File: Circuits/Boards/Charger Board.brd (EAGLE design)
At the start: 63.5 x 50.8 mm, 67 parts, among them CON1 ISP(2X3), CON10 HEADER_3X1, CON11 HEADER_3X1, CON12 HEADER_3X1, CON3 HEADER_3X1, CON4 HEADER_3X1, CON5 HEADER_3X1, CON6 HEADER_3X1, CON7 HEADER_3X1, CON8 HEADER_3X1, CON9 HEADER_3X1, IC1 NCP1117DT33G, T1 NPN2N2222, T2 NPN2N2222, T3 SI4421DY, U1 ATMEGA324P, U2 ACS711

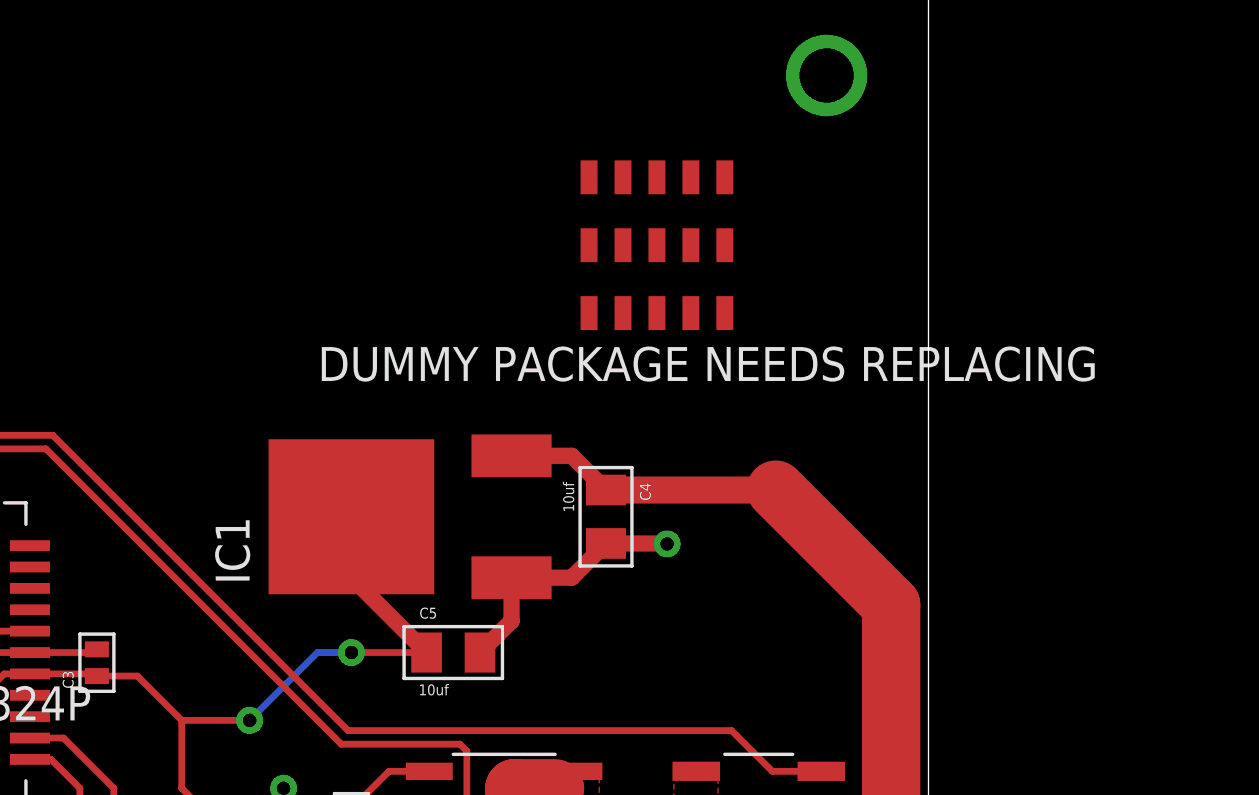
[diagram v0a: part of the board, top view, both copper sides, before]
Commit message: 
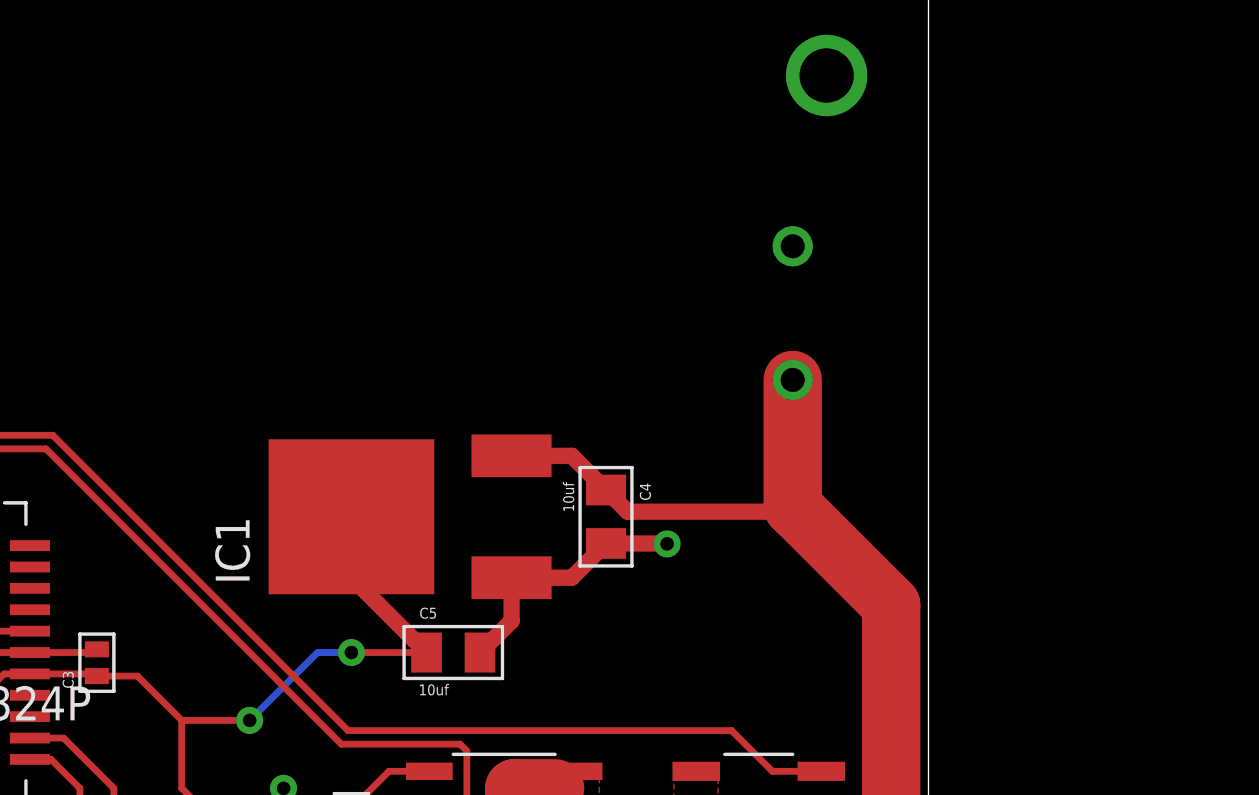
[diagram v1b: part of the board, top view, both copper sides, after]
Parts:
- removed S1: ROCKER_SWITCH, Mechanical:DUMMY
- added CON2: SCREWTERMINAL_1X2, Mechanical:SCREWTERMINAL_1X2
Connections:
- removed net VIN: S1.P$2
- net +5V: now also CON2.1; no longer S1.P$3
- net GND: now also CON2.2
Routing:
- net +5V: track 28.8 -> 33.8 mm
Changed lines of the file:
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@@
 <element name="R27" library="Passive" package="0603" value="470" x="52.705" y="12.7" rot="R90"/>
 <element name="R28" library="Passive" package="0603" value="" x="8.89" y="35.56" rot="R180"/>
-<element name="S1" library="Mechanical" package="DUMMY" value="ROCKER_SWITCH" x="53.34" y="40.64" rot="R180"/>
 <element name="U2" library="PowerIC" package="8SOIC" value="ACS711" x="47.625" y="19.05" rot="R90"/>
 <element name="C1" library="Passive" package="0603" value=".1uf" x="41.91" y="19.05" rot="R90"/>
@@
 <element name="H3" library="Mechanical" package="MOUNTINGHOLE" value="MOUNTINGHOLE" x="59.69" y="46.99"/>
 <element name="H4" library="Mechanical" package="MOUNTINGHOLE" value="MOUNTINGHOLE" x="59.69" y="3.81"/>
+<element name="CON2" library="Mechanical" package="SCREWTERMINAL_1X2" value="SCREWTERMINAL_1X2" x="58.42" y="38.1" rot="R90"/>
 </elements>
 <signals>
@@
 <wire x1="11.16" y1="37.1" x2="11.43" y2="36.83" width="0.254" layer="1"/>
 <via x="11.43" y="36.83" extent="1-16" drill="0.508"/>
+<contactref element="CON2" pad="2"/>
 <wire x1="9.84" y1="37.1" x2="-18.05" y2="68.58" width="0" layer="19" extent="1-1"/>
 <wire x1="-70.8" y1="61.96" x2="-18.05" y2="68.58" width="0" layer="19" extent="1-1"/>
@@
 <contactref element="T3" pad="2"/>
 <contactref element="T3" pad="3"/>
-<contactref element="S1" pad="P$3"/>
 <contactref element="IC1" pad="3"/>
 <contactref element="C4" pad="1"/>
@@
 <wire x1="61.341" y1="18.415" x2="62.103" y2="19.304" width="2.1844" layer="1"/>
 <wire x1="62.103" y1="19.304" x2="62.103" y2="27.178" width="2.1844" layer="1"/>
-<wire x1="62.103" y1="27.178" x2="57.785" y2="31.496" width="2.1844" layer="1"/>
-<wire x1="51.435" y1="31.48" x2="57.769" y2="31.48" width="1.016" layer="1"/>
-<wire x1="57.769" y1="31.48" x2="57.785" y2="31.496" width="1.016" layer="1"/>
-<wire x1="50.155" y1="32.76" x2="54.61" y2="38.1" width="0" layer="19" extent="1-1"/>
+<contactref element="CON2" pad="1"/>
+<wire x1="62.103" y1="27.178" x2="58.6105" y2="30.6705" width="2.1844" layer="1"/>
+<wire x1="58.6105" y1="30.6705" x2="58.42" y2="30.861" width="2.1844" layer="1"/>
+<wire x1="58.42" y1="30.861" x2="58.42" y2="35.6" width="2.1844" layer="1"/>
+<wire x1="51.435" y1="31.48" x2="52.2445" y2="30.6705" width="0.6096" layer="1"/>
+<wire x1="52.2445" y1="30.6705" x2="58.6105" y2="30.6705" width="0.6096" layer="1"/>
 </signal>
 <signal name="CURRENTSENSE">
@@
 <wire x1="33.02" y1="17.645" x2="36.83" y2="13.835" width="0.254" layer="1"/>
 </signal>
-<signal name="VIN">
-<contactref element="S1" pad="P$2"/>
-</signal>
 <signal name="N$12">

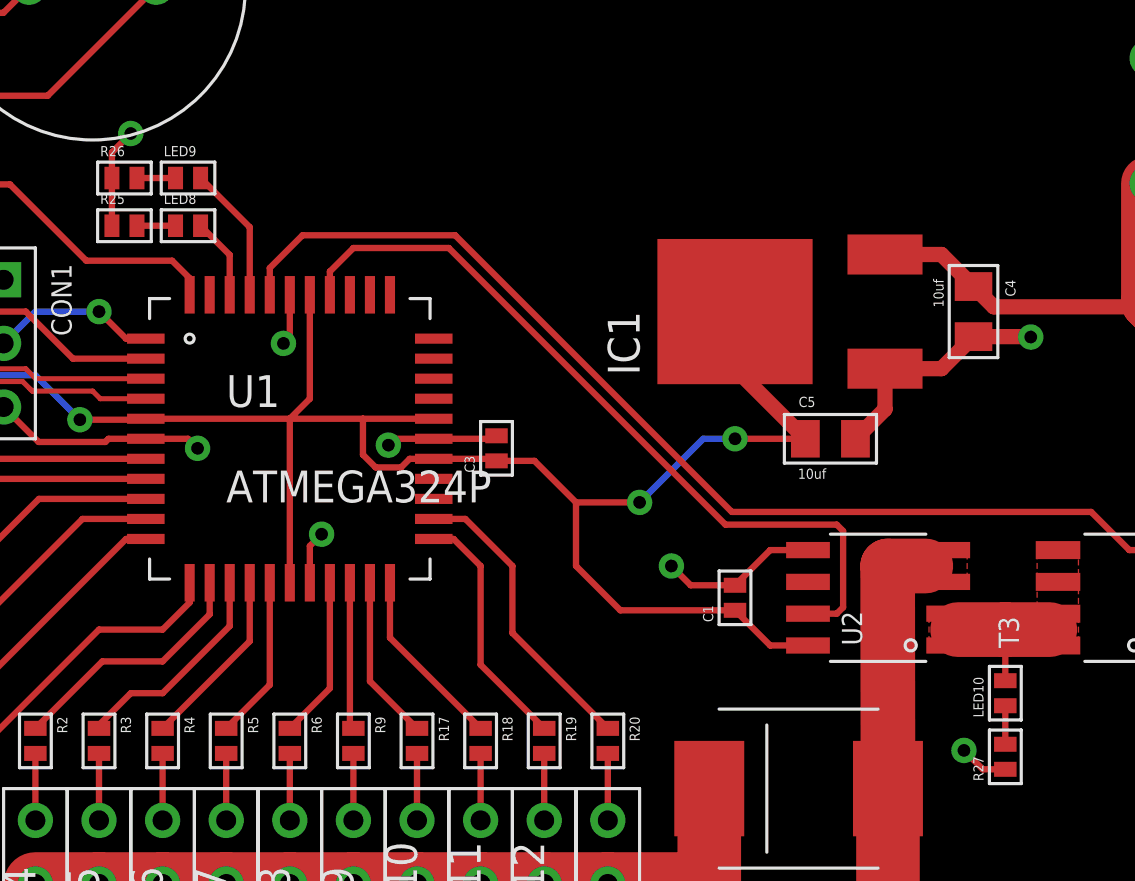
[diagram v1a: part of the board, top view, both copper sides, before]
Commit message: 
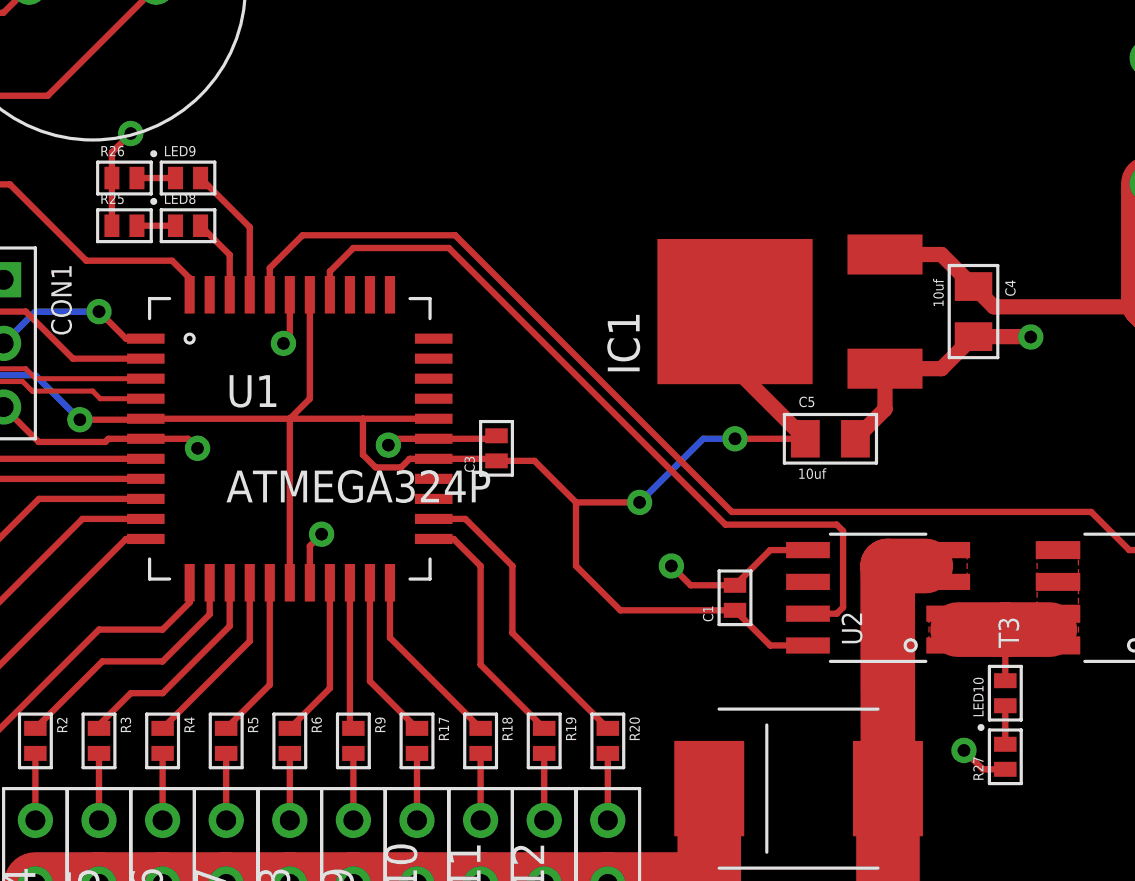
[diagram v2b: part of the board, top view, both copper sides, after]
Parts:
- LED10, LED8, LED9: device Passive:0603 -> Passive:LED0603
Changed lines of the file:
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@@
 <element name="LED7" library="Passive" package="5MM_LED_RA" value="IR" x="-35.56" y="20.32"/>
 <element name="C6" library="Passive" package="0805" value="10uf" x="-19.05" y="68.58"/>
-<element name="LED8" library="Passive" package="0603" value="" x="20.066" y="33.909"/>
+<element name="LED8" library="Passive" package="LED0603" value="" x="20.066" y="33.909"/>
 <element name="R25" library="Passive" package="0603" value="200" x="17.526" y="33.909"/>
-<element name="LED9" library="Passive" package="0603" value="" x="20.066" y="35.814"/>
+<element name="LED9" library="Passive" package="LED0603" value="" x="20.066" y="35.814"/>
 <element name="R26" library="Passive" package="0603" value="200" x="17.526" y="35.814"/>
-<element name="LED10" library="Passive" package="0603" value="" x="52.705" y="15.24" rot="R90"/>
+<element name="LED10" library="Passive" package="LED0603" value="" x="52.705" y="15.24" rot="R90"/>
 <element name="R27" library="Passive" package="0603" value="470" x="52.705" y="12.7" rot="R90"/>
 <element name="R28" library="Passive" package="0603" value="" x="8.89" y="35.56" rot="R180"/>
